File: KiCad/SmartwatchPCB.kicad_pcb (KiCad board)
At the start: 2 copper layers, 28.4 x 40 mm, 10 parts, among them IC1 ATSAML22G18A-MUT

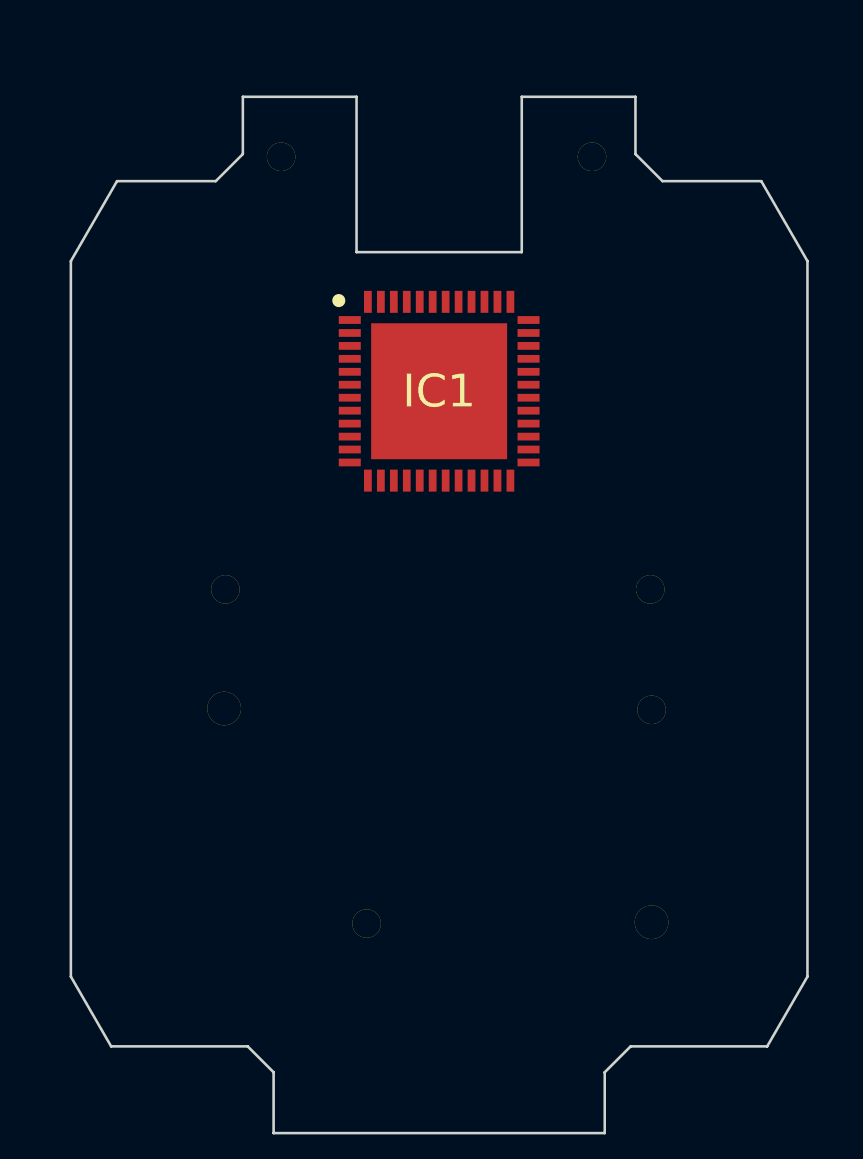
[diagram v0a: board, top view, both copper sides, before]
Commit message: added button and lcd parts and sprinkled them
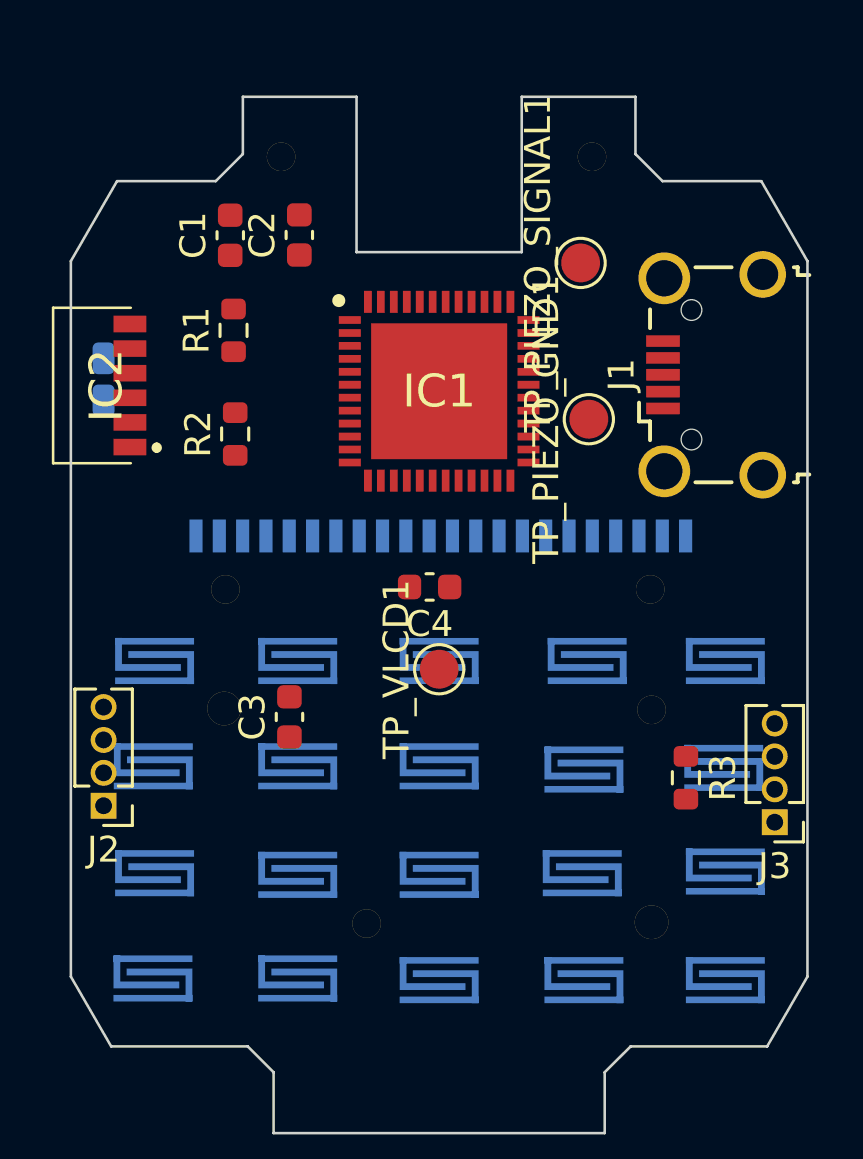
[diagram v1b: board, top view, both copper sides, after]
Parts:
- added C1: 100nF, Capacitor_SMD:C_0603_1608Metric, F.Cu at (-8.06, -14.7)
- added C2: 10uF, Capacitor_SMD:C_0603_1608Metric, F.Cu at (-5.40, -14.7)
- added C3: 1uF, Capacitor_SMD:C_0603_1608Metric, F.Cu at (-5.78, 3.94)
- added C4: 1uF, Capacitor_SMD:C_0603_1608Metric, F.Cu at (-0.37, -1.08)
- added D1: LED, LED_SMD:LED_0603_1608Metric_Castellated, B.Cu at (-13.0, -9.09)
- added IC2: TFBS4711-TT1, TFBS4711-TT1:TFBS4711TT1, F.Cu at (-13.4, -8.86)
- added J1: USB_B_Micro, Connector_USB:USB_Micro-B_Wuerth_629105150521_CircularHoles, F.Cu at (10.5, -9.27)
- added J2: Conn_01x04_Male, Connector_PinHeader_1.27mm:PinHeader_1x04_P1.27mm_Vertical, F.Cu at (-13.0, 7.37)
- added J3: Conn_01x04_Male, Connector_PinHeader_1.27mm:PinHeader_1x04_P1.27mm_Vertical, F.Cu at (13.0, 8.00)
- added R1: R, Resistor_SMD:R_0603_1608Metric, F.Cu at (-7.94, -11.0)
- added R2: R, Resistor_SMD:R_0603_1608Metric, F.Cu at (-7.87, -6.99)
- added R3: R, Resistor_SMD:R_0603_1608Metric, F.Cu at (9.53, 6.29)
- added SW_0: SW_Push, SmartwatchPCB:button, B.Cu at (5.59, 13.8)
- added SW_1: SW_Push, SmartwatchPCB:button, B.Cu at (5.52, 9.72)
- added SW_2: SW_Push, SmartwatchPCB:button, B.Cu at (0.00, 9.78)
- added SW_3: SW_Push, SmartwatchPCB:button, B.Cu at (-5.46, 9.78)
- added SW_4: SW_Push, SmartwatchPCB:button, B.Cu at (5.59, 5.71)
- added SW_5: SW_Push, SmartwatchPCB:button, B.Cu at (0.00, 5.59)
- added SW_6: SW_Push, SmartwatchPCB:button, B.Cu at (-5.46, 5.59)
- added SW_7: SW_Push, SmartwatchPCB:button, B.Cu at (-5.46, 1.52)
- added SW_8: SW_Push, SmartwatchPCB:button, B.Cu at (0.00, 1.52)
- added SW_9: SW_Push, SmartwatchPCB:button, B.Cu at (5.71, 1.52)
- added SW_ADD1: SW_Push, SmartwatchPCB:button, B.Cu at (-11.0, 14.3)
- added SW_DIV1: SW_Push, SmartwatchPCB:button, B.Cu at (-11.0, 1.52)
- added SW_DOT1: SW_Push, SmartwatchPCB:button, B.Cu at (0.00, 13.8)
- added SW_EQ1: SW_Push, SmartwatchPCB:button, B.Cu at (-5.46, 13.8)
- added SW_M1: SW_Push, SmartwatchPCB:button, B.Cu at (11.0, 5.65)
- added SW_MUL1: SW_Push, SmartwatchPCB:button, B.Cu at (-11.0, 5.59)
- added SW_ON1: SW_Push, SmartwatchPCB:button, B.Cu at (11.0, 13.8)
- added SW_S1: SW_Push, SmartwatchPCB:button, B.Cu at (11.0, 1.52)
- added SW_SQRT1: SW_Push, SmartwatchPCB:button, B.Cu at (11.0, 9.65)
- added SW_SUB1: SW_Push, SmartwatchPCB:button, B.Cu at (-11.0, 9.72)
- added TP_PIEZO_GND1: TestPoint, TestPoint:TestPoint_Pad_D1.5mm, F.Cu at (5.78, -7.56)
- added TP_PIEZO_SIGNAL1: TestPoint, TestPoint:TestPoint_Pad_D1.5mm, F.Cu at (5.46, -13.6)
- added TP_VLCD1: TestPoint, TestPoint:TestPoint_Pad_D1.5mm, F.Cu at (0.00, 2.10)
- added U1: LCD, SmartwatchPCB:display, B.Cu at (0.06, -3.05)
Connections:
- IC1 pad 17: Net-(IC1-Pad17) -> VCC
- IC1 pad 18: Net-(IC1-Pad18) -> GND
- IC1 pad 19: Net-(IC1-Pad19) -> VCC_LCD
- IC1 pad 3: Net-(IC1-Pad3) -> KEYPAD_1
- IC1 pad 32: Net-(IC1-Pad32) -> KEYPAD_3
- IC1 pad 35: Net-(IC1-Pad35) -> GND
- IC1 pad 36: Net-(IC1-Pad36) -> VCC
- IC1 pad 4: Net-(IC1-Pad4) -> KEYPAD_2
- IC1 pad 41: Net-(IC1-Pad41) -> VCC_CORE
- IC1 pad 42: Net-(IC1-Pad42) -> GND
- IC1 pad 44: Net-(IC1-Pad44) -> VCC
- IC1 pad 45: Net-(IC1-Pad45) -> SWCLK
- IC1 pad 46: Net-(IC1-Pad46) -> SWDIO
- IC1 pad 47: Net-(IC1-Pad47) -> SDA
- IC1 pad 48: Net-(IC1-Pad48) -> SCL
- IC1 pad 49: Net-(IC1-Pad49) -> GND
- IC1 pad 5: Net-(IC1-Pad5) -> GND
- IC1 pad 6: Net-(IC1-Pad6) -> VCC

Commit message: anything to commit?
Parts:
- added kibuzzard-60FD6129: G***, label, B.Cu at (0.00, 18.2)
- moved SW_9 11.2 mm to (-5.52, 1.52)
- moved SW_7 11.1 mm to (5.65, 1.52)

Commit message: started to wire up things
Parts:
- moved C4 29.5 mm to (28.4, 5.66)
- moved C3 29.2 mm to (23.4, 6.24)
- moved TP_PIEZO_GND1 8.93 mm to (10.5, -15.1)
- moved SW_ADD1 0.48 mm to (-11.0, 13.8), turned to 0 degrees
- moved IC1 0.25 mm to (0.00, -8.38)
- moved SW_7 0.17 mm to (5.49, 1.52)
- moved SW_SQRT1 0.13 mm to (11.0, 9.78), turned to 180 degrees
- moved SW_4 0.13 mm to (5.49, 5.64)
- moved SW_0 0.10 mm to (5.49, 13.8), turned to 180 degrees
- moved SW_1 0.07 mm to (5.49, 9.78), turned to 180 degrees
- moved SW_SUB1 0.06 mm to (-11.0, 9.78)
- moved SW_MUL1 0.06 mm to (-11.0, 5.59)
- turned SW_EQ1 to 180 degrees
- turned SW_ON1 to 180 degrees
- turned SW_DOT1 to 180 degrees
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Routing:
- net KEYPAD_3: track 0.00 -> 43.3 mm, vias 0 -> 5
- net KEYPAD_2: track 0.00 -> 41.2 mm, vias 0 -> 4
- net SWDIO: track 0.00 -> 39.9 mm, vias 0 -> 4
- net SWCLK: track 0.00 -> 37.2 mm, vias 0 -> 3
- net KEYPAD_1: track 0.00 -> 32.3 mm
- net Net-(IC1-Pad31): track 0.00 -> 12.5 mm, vias 0 -> 1
- net Net-(IC1-Pad30): track 0.00 -> 11.6 mm, vias 0 -> 1
- net Net-(IC1-Pad7): track 0.00 -> 9.52 mm, vias 0 -> 1
- net Net-(IC1-Pad29): track 0.00 -> 9.31 mm, vias 0 -> 1
- net Net-(IC1-Pad10): track 0.00 -> 9.25 mm, vias 0 -> 1
- net Net-(IC1-Pad28): track 0.00 -> 8.79 mm, vias 0 -> 1
- net Net-(IC1-Pad9): track 0.00 -> 8.68 mm, vias 0 -> 1
- net Net-(IC1-Pad20): track 0.00 -> 8.62 mm, vias 0 -> 1
- net Net-(IC1-Pad8): track 0.00 -> 8.37 mm, vias 0 -> 1
- net Net-(IC1-Pad26): track 0.00 -> 8.04 mm, vias 0 -> 1
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- added copper zone on F.Cu, net (none)
- added copper zone on B.Cu, net GND

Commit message: more routing and footprint updates
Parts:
- added L1: L, Inductor_SMD:L_0603_1608Metric, F.Cu at (-0.03, -13.3)
- J2: footprint Connector_PinHeader_1.27mm:PinHeader_1x04_P1.27mm_Vertical -> Connector_JST:JST_SH_SM04B-SRSS-TB_1x04-1MP_P1.00mm_Horizontal
- moved J2 2.01 mm to (-10.9, 7.45), turned to 270 degrees
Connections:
- J1 pad 2: Net-(IC1-Pad33) -> Net-(J1-Pad2)
- J1 pad 3: Net-(IC1-Pad34) -> Net-(J1-Pad3)
- R1 pad 1: Net-(IC1-Pad38) -> Net-(R1-Pad1)
- R2 pad 1: Net-(IC2-Pad1) -> Net-(R2-Pad1)
- TP_PIEZO_SIGNAL1 pad 1: Net-(IC1-Pad37) -> Net-(TP_PIEZO_SIGNAL1-Pad1)
- U1 pad 1: Net-(IC1-Pad31) -> Net-(U1-Pad1)
- U1 pad 10: Net-(IC1-Pad22) -> Net-(U1-Pad10)
- U1 pad 11: Net-(IC1-Pad21) -> Net-(U1-Pad11)
- U1 pad 12: Net-(IC1-Pad20) -> Net-(U1-Pad12)
- U1 pad 13: Net-(IC1-Pad16) -> Net-(U1-Pad13)
- U1 pad 14: Net-(IC1-Pad15) -> Net-(U1-Pad14)
- U1 pad 15: Net-(IC1-Pad14) -> Net-(U1-Pad15)
- U1 pad 16: Net-(IC1-Pad13) -> Net-(U1-Pad16)
- U1 pad 17: Net-(IC1-Pad12) -> Net-(U1-Pad17)
- U1 pad 18: Net-(IC1-Pad11) -> Net-(U1-Pad18)
- U1 pad 19: Net-(IC1-Pad10) -> Net-(U1-Pad19)
- U1 pad 2: Net-(IC1-Pad30) -> Net-(U1-Pad2)
- U1 pad 20: Net-(IC1-Pad9) -> Net-(U1-Pad20)
- U1 pad 21: Net-(IC1-Pad8) -> Net-(U1-Pad21)
- U1 pad 22: Net-(IC1-Pad7) -> Net-(U1-Pad22)
- U1 pad 3: Net-(IC1-Pad29) -> Net-(U1-Pad3)
- U1 pad 4: Net-(IC1-Pad28) -> Net-(U1-Pad4)
- U1 pad 5: Net-(IC1-Pad27) -> Net-(U1-Pad5)
- U1 pad 6: Net-(IC1-Pad26) -> Net-(U1-Pad6)
- U1 pad 7: Net-(IC1-Pad25) -> Net-(U1-Pad7)
- U1 pad 8: Net-(IC1-Pad24) -> Net-(U1-Pad8)
- U1 pad 9: Net-(IC1-Pad23) -> Net-(U1-Pad9)

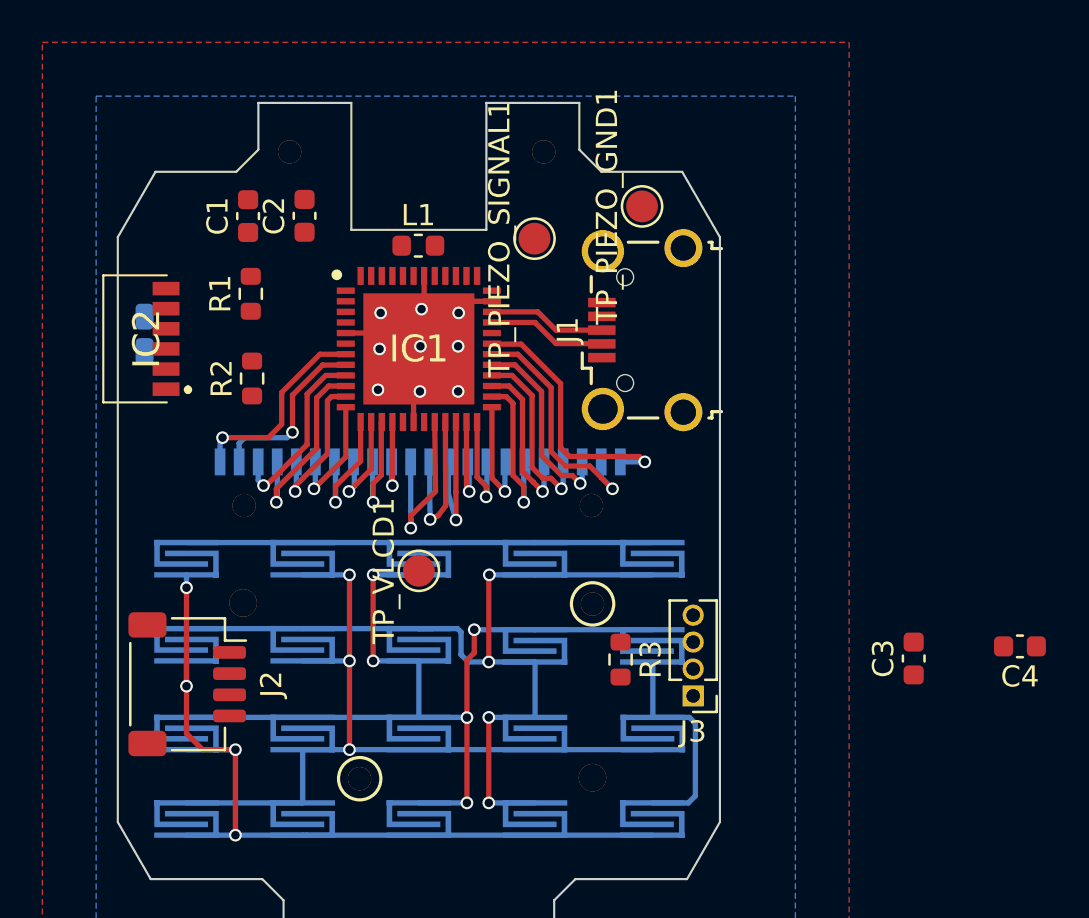
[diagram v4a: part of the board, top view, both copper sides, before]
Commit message: footprint and symbol libraries updated
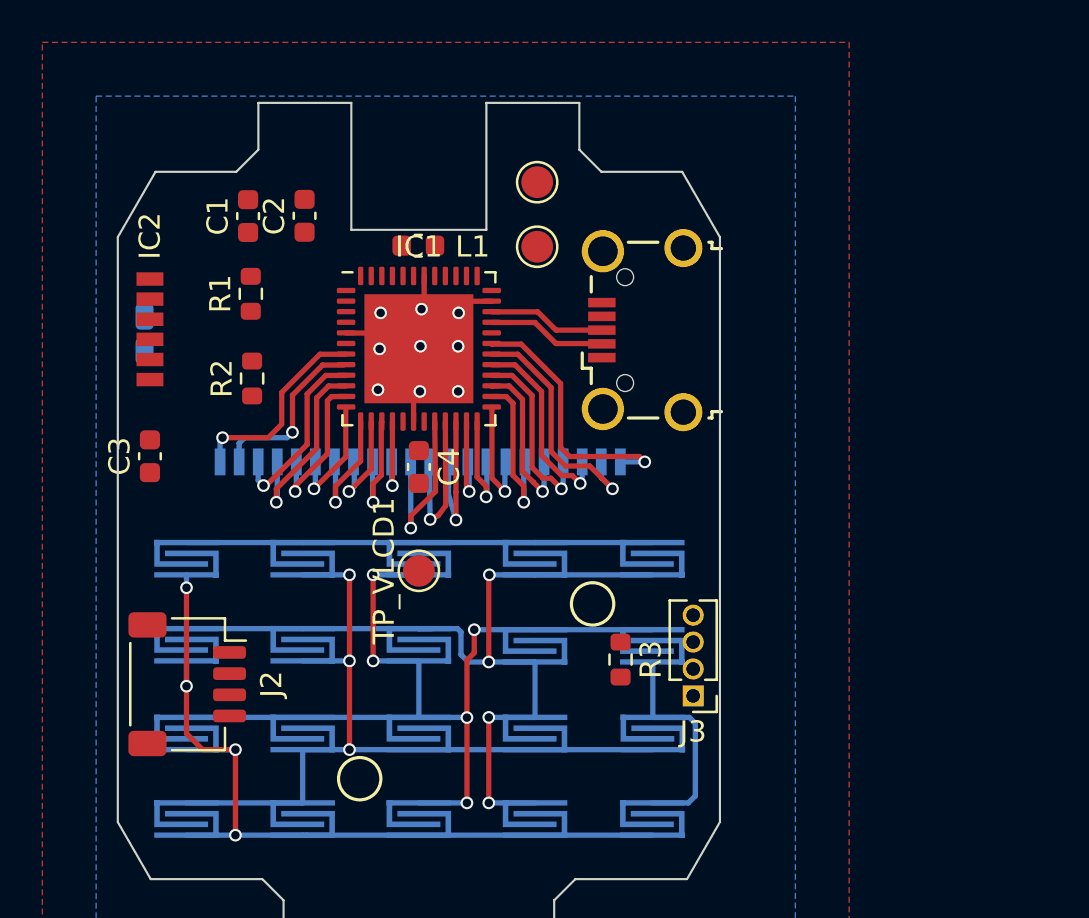
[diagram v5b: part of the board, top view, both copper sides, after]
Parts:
- removed ? (x8): , Wire_Pads:SolderWirePad_single_0-8mmDrill
- removed G***: LOGO, LOGO
- removed kibuzzard-60FD6129: G***, label
- IC1: value ATSAML22G18A-MUT -> SAML22G; footprint ATSAML22G18A-MUT:QFN50P700X700X90-49N-D -> Package_DFN_QFN:QFN-48-1EP_7x7mm_P0.5mm_EP5.15x5.15mm
- IC2: value TFBS4711-TT1 -> TFBS4711; footprint TFBS4711-TT1:TFBS4711TT1 -> SmartwatchPCB:TFBS4711
- moved C3 37.3 mm to (-12.7, -3.31)
- moved C4 29.6 mm to (0.00, -2.81), turned to 270 degrees
- moved TP_PIEZO_GND1 5.08 mm to (5.59, -16.3)
- moved IC2 0.84 mm to (-12.7, -9.31), turned to 270 degrees
- moved TP_PIEZO_SIGNAL1 0.40 mm to (5.59, -13.2)
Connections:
- net Net-(IC1-Pad1) renamed IR_RX
- net Net-(IC1-Pad2) renamed IR_TX
- IC1 pad 37: Net-(IC1-Pad37) -> PIEZO
- IC1 pad 38: Net-(IC1-Pad38) -> LEDbacklight
- IC1 pad 39: Net-(IC1-Pad39) -> IR_MODE
- IC1 pad 43: Net-(IC1-Pad43) -> VDD_OUT
- IC2 pad 4: Net-(IC2-Pad4) -> IR_MODE
- J1 pad 2: Net-(J1-Pad2) -> Net-(IC1-Pad33)
- J1 pad 3: Net-(J1-Pad3) -> Net-(IC1-Pad34)
- R1 pad 1: Net-(R1-Pad1) -> LEDbacklight
- R2 pad 1: Net-(R2-Pad1) -> Net-(IC2-Pad1)
- TP_PIEZO_SIGNAL1 pad 1: Net-(TP_PIEZO_SIGNAL1-Pad1) -> PIEZO
- U1 pad 1: Net-(U1-Pad1) -> Net-(IC1-Pad31)
- U1 pad 10: Net-(U1-Pad10) -> Net-(IC1-Pad22)
- U1 pad 11: Net-(U1-Pad11) -> Net-(IC1-Pad21)
- U1 pad 12: Net-(U1-Pad12) -> Net-(IC1-Pad20)
- U1 pad 13: Net-(U1-Pad13) -> Net-(IC1-Pad16)
- U1 pad 14: Net-(U1-Pad14) -> Net-(IC1-Pad15)
- U1 pad 15: Net-(U1-Pad15) -> Net-(IC1-Pad14)
- U1 pad 16: Net-(U1-Pad16) -> Net-(IC1-Pad13)
- U1 pad 17: Net-(U1-Pad17) -> Net-(IC1-Pad12)
- U1 pad 18: Net-(U1-Pad18) -> Net-(IC1-Pad11)
- U1 pad 19: Net-(U1-Pad19) -> Net-(IC1-Pad10)
- U1 pad 2: Net-(U1-Pad2) -> Net-(IC1-Pad30)
- U1 pad 20: Net-(U1-Pad20) -> Net-(IC1-Pad9)
- U1 pad 21: Net-(U1-Pad21) -> Net-(IC1-Pad8)
- U1 pad 22: Net-(U1-Pad22) -> Net-(IC1-Pad7)
- U1 pad 3: Net-(U1-Pad3) -> Net-(IC1-Pad29)
- U1 pad 4: Net-(U1-Pad4) -> Net-(IC1-Pad28)
- U1 pad 5: Net-(U1-Pad5) -> Net-(IC1-Pad27)
- U1 pad 6: Net-(U1-Pad6) -> Net-(IC1-Pad26)
- U1 pad 7: Net-(U1-Pad7) -> Net-(IC1-Pad25)
- U1 pad 8: Net-(U1-Pad8) -> Net-(IC1-Pad24)
- U1 pad 9: Net-(U1-Pad9) -> Net-(IC1-Pad23)

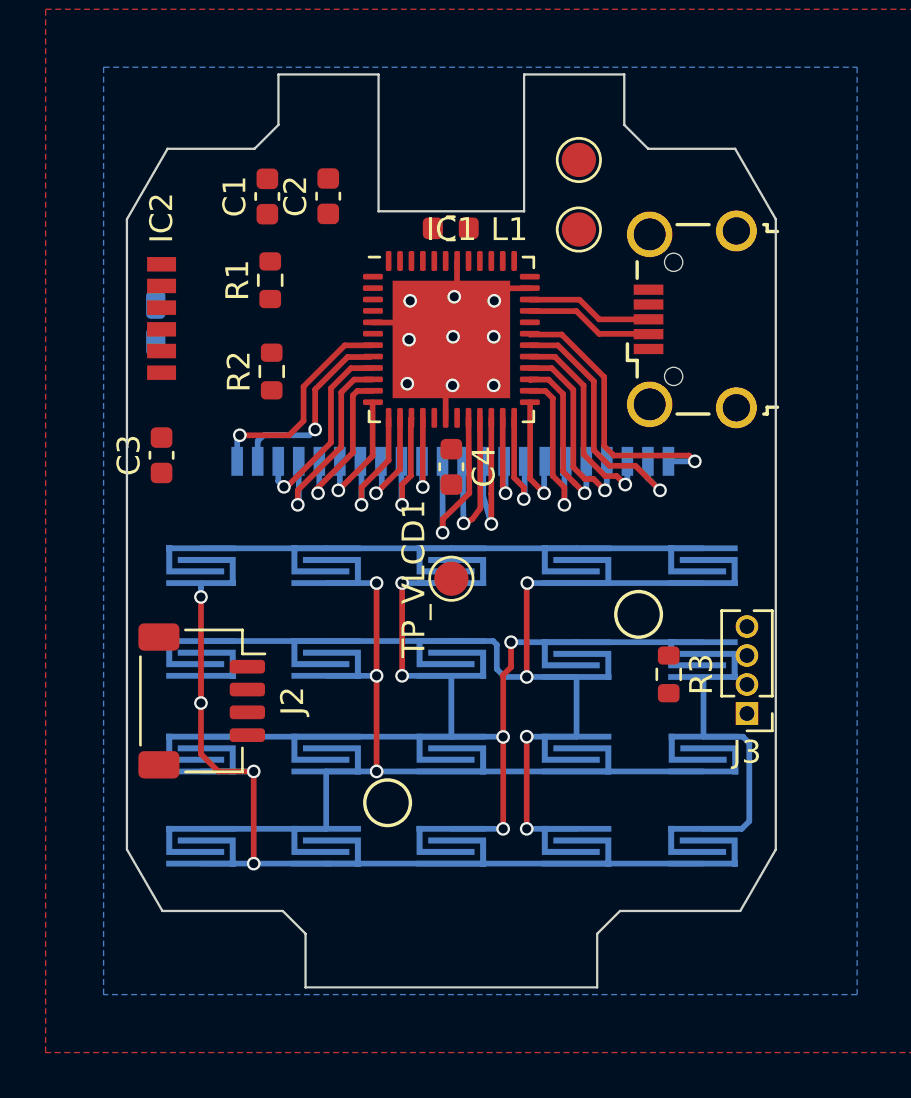
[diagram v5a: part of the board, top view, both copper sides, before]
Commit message: moved IC, more wiring
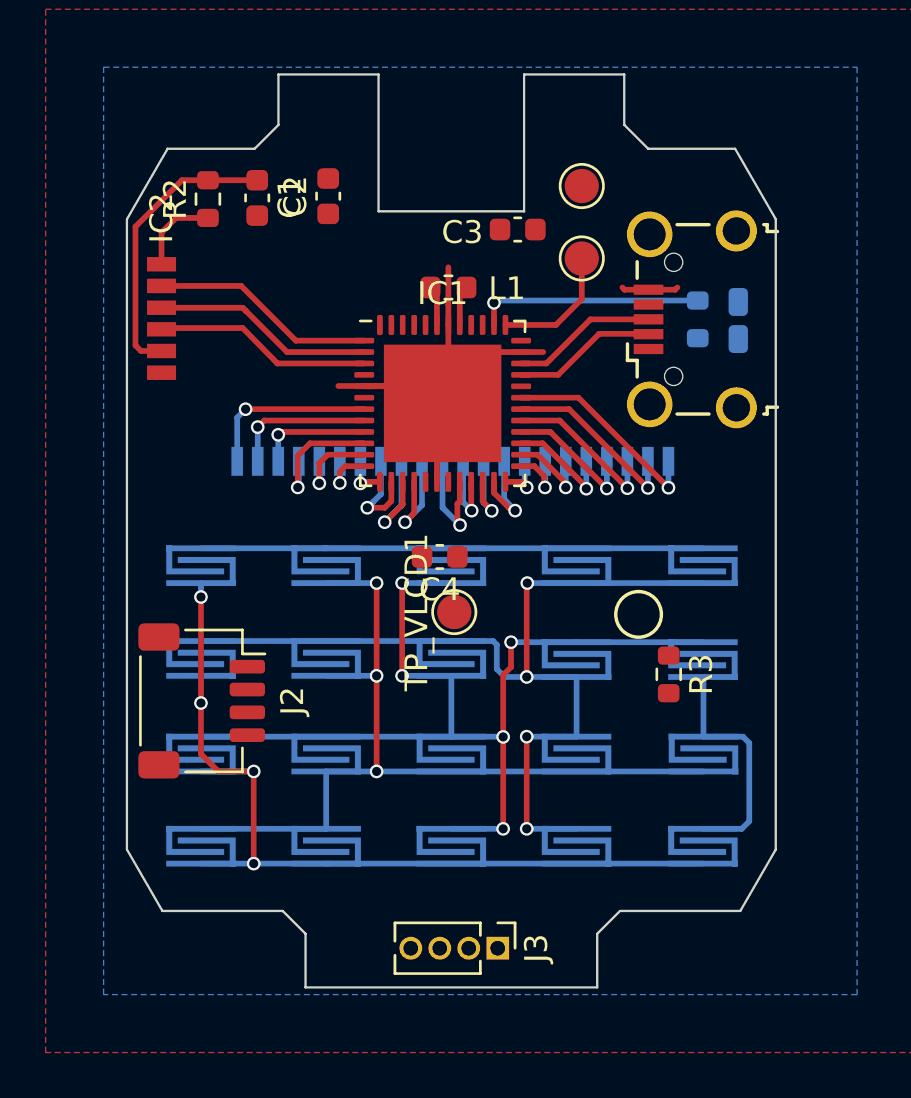
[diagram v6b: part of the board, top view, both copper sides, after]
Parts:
- R1: moved to B.Cu
- moved D1 25.5 mm to (12.6, -9.22)
- moved R1 18.8 mm to (10.8, -9.27), turned to 270 degrees
- moved C3 18.5 mm to (2.91, -13.2), turned to 0 degrees
- moved J3 15.0 mm to (2.03, 18.3), turned to 270 degrees
- moved R2 8.06 mm to (-10.7, -14.5)
- moved C4 3.98 mm to (-0.51, 1.14), turned to 180 degrees
- moved IC1 2.83 mm to (-0.38, -5.59)
- moved L1 2.59 mm to (-0.13, -10.7)
- moved TP_VLCD1 1.47 mm to (0.13, 3.56)
- moved TP_PIEZO_SIGNAL1 1.28 mm to (5.71, -11.9)
- moved TP_PIEZO_GND1 1.15 mm to (5.71, -15.1)
- moved C1 0.45 mm to (-8.51, -14.6), turned to 270 degrees
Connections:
- IC1 pad 1: IR_RX -> IR_TX
- IC1 pad 2: IR_TX -> IR_RX
- IC1 pad 3: KEYPAD_1 -> IR_MODE
- IC1 pad 39: IR_MODE -> KEYPAD_1
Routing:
- net VCC: track 0.00 -> 12.6 mm
- net LEDbacklight: track 0.00 -> 9.94 mm, vias 0 -> 1
- net IR_TX: track 0.00 -> 9.87 mm
- net IR_RX: track 0.00 -> 9.69 mm
- net IR_MODE: track 0.00 -> 9.53 mm
- net GND: track 6.15 -> 12.8 mm, vias 9 -> 0
- net PIEZO: track 0.00 -> 5.59 mm
- net Net-(IC1-Pad26): track 8.04 -> 3.81 mm
- net Net-(IC1-Pad13): track 6.06 -> 1.85 mm
- net Net-(IC1-Pad22): track 7.93 -> 3.76 mm
- net Net-(IC1-Pad21): track 7.68 -> 3.58 mm
- net Net-(IC2-Pad1): track 0.00 -> 3.69 mm
- net Net-(IC1-Pad10): track 9.25 -> 5.69 mm
- net Net-(IC1-Pad9): track 8.68 -> 5.13 mm
- net Net-(IC1-Pad20): track 8.62 -> 5.10 mm
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- added copper zone on F.Cu, net GND
- removed copper zone on F.Cu, net (none)
